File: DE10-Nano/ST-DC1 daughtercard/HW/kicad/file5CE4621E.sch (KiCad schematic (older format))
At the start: 18 parts, among them J10 ENC1_IN, J27 ENC2_IN, J3 ENC0_IN, J30 ENC3_IN, J33 ENC4_IN, J36 ENC5_IN, U1 AM26LS32, U10 AM26LS32, U11 AM26LS32, U12 AM26LS32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

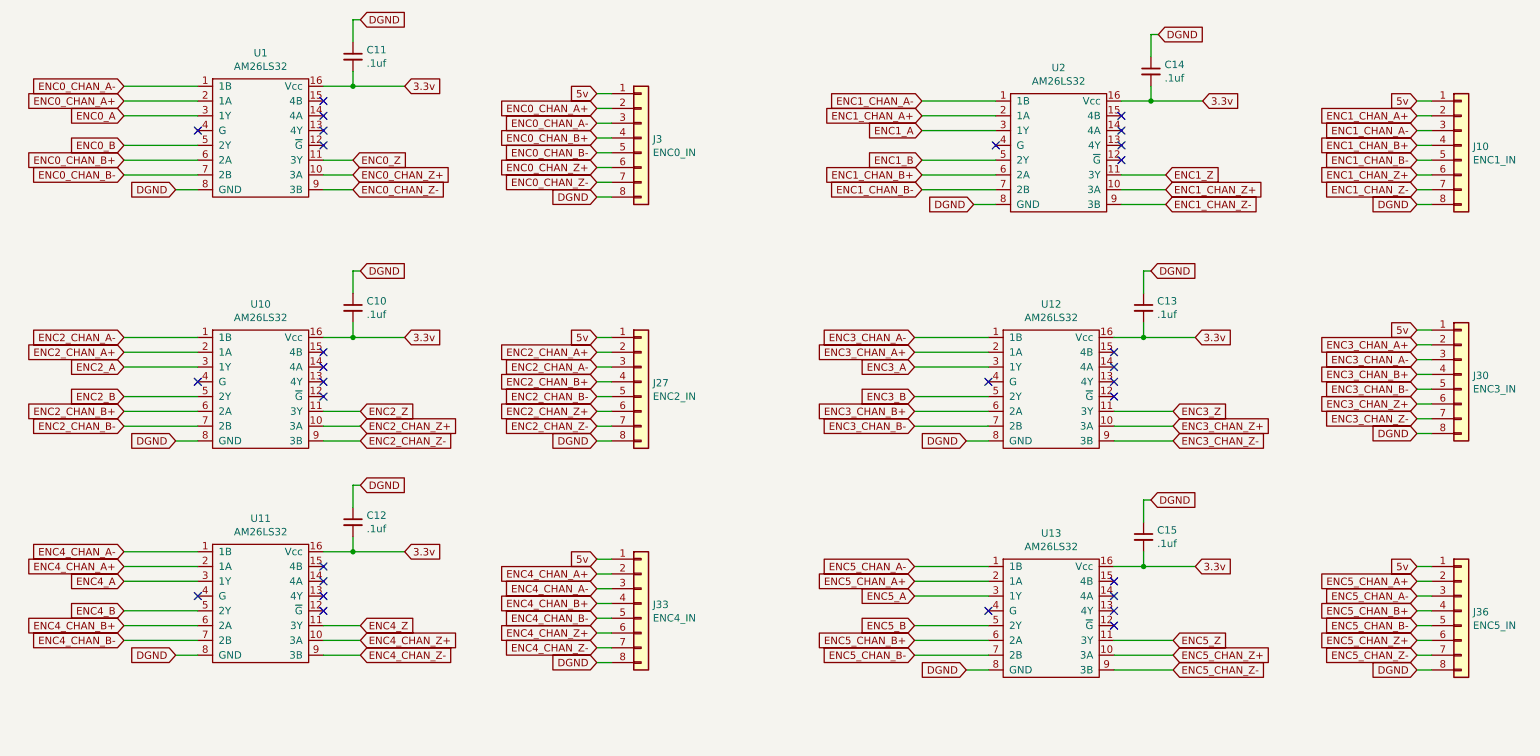
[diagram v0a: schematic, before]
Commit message: Add Artwork to PCB:   DE10-Nano/ST-DC1 daughtercard/HW/kicad/DE10nano interface-cache.lib 	Add Artwork to PCB:    DE10-Nano/ST-DC1 daughtercard/HW/kicad/DE10nano interface.jpg 	Add termination Resistors to diff inputs:   DE10-Nano/ST-DC1 daughtercard/HW/kicad/DE10nano interface.kicad_pcb 	Add termination Resistors to diff inputs:   DE10-Nano/ST-DC1 daughtercard/HW/kicad/DE10nano interface.kicad_pcb-bak 	Add termination Resistors to diff inputs:   DE10-Nano/ST-DC1 daughtercard/HW/kicad/DE10nano interface.net 	Add termination Resistors to diff inputs:   DE10-Nano/ST-DC1 daughtercard/HW/kicad/DE10nano interface.pro 	Add termination Resistors to diff inputs:   DE10-Nano/ST-DC1 daughtercard/HW/kicad/Images/DE10nano interface back.jpg 	Add Artwork to PCB:   DE10-Nano/ST-DC1 daughtercard/HW/kicad/Images/DE10nano interface.jpg 	Reflect incomplete BOM:    DE10-Nano/ST-DC1 daughtercard/HW/kicad/bom/BOM.ods -> DE10-Nano/ST-DC1 daughtercard/HW/kicad/bom/BOM-incomplete-use-ibom.ods 	Add termination Resistors to diff inputs:   DE10-Nano/ST-DC1 daughtercard/HW/kicad/bom/ibom.html 	Add termination Resistors to diff inputs:   DE10-Nano/ST-DC1 daughtercard/HW/kicad/file5CE4621E.sch 	Add termination Resistors to diff inputs:   DE10-Nano/ST-DC1 daughtercard/HW/kicad/file5CE4621E.sch-bak 	Add termination Resistors to diff inputs:   DE10-Nano/ST-DC1 daughtercard/HW/kicad/file5D10B445.sch-bak 	Add termination Resistors to diff inputs:   DE10-Nano/ST-DC1 daughtercard/HW/kicad/file5D22A4F0.sch 	modified:   DE10-Nano/ST-DC1 daughtercard/HW/kicad/file5D22A4F0.sch-bak 	modified:   DE10-Nano/ST-DC1 daughtercard/HW/kicad/gerbers rev_G.zip 	modified:   DE10-Nano/ST-DC1 daughtercard/HW/kicad/gerbers rev_G/DE10nano interface-B_Cu.gbr 	modified:   DE10-Nano/ST-DC1 daughtercard/HW/kicad/gerbers rev_G/DE10nano interface-B_Mask.gbr 	modified:   DE10-Nano/ST-DC1 daughtercard/HW/kicad/gerbers rev_G/DE10nano interface-B_Paste.gbr 	modified:   DE10-Nano/ST-DC1 daughtercard/HW/kicad/gerbers rev_G/DE10nano i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
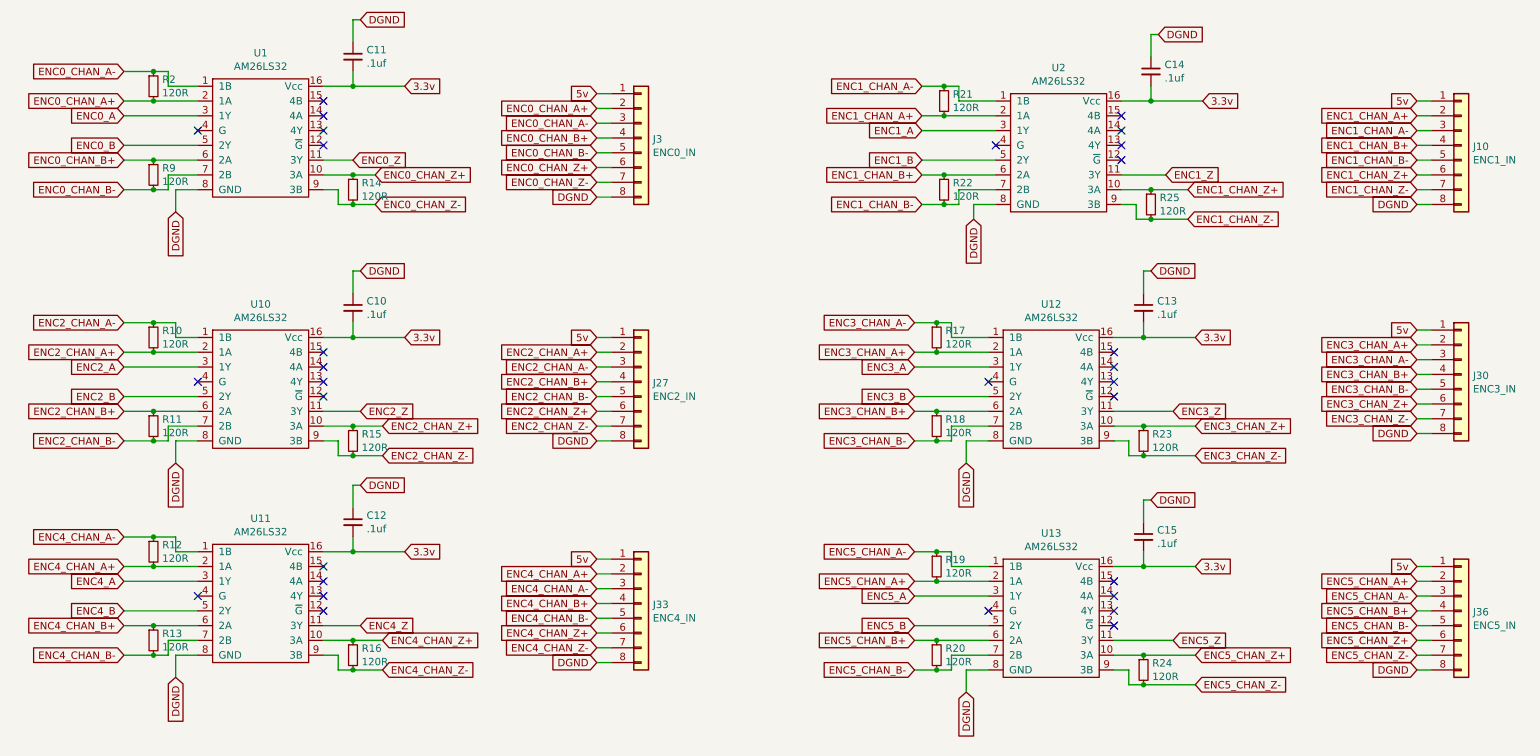
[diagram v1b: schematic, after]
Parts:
- added R10, R11, R12, R13, R14, R15, R16, R17, R18, R19, R2, R20, R21, R22, R23, R24, R25, R9: 120R, Resistor_SMD:R_0805_2012Metric, symbol Device:R_Small
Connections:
- net ENC0_CHAN_A+: now also R2.2
- net ENC0_CHAN_A-: now also R2.1
- net ENC0_CHAN_B+: now also R9.1
- net ENC0_CHAN_B-: now also R9.2
- net ENC0_CHAN_Z+: now also R14.1
- net ENC0_CHAN_Z-: now also R14.2
- net ENC1_CHAN_A+: now also R21.2
- net ENC1_CHAN_A-: now also R21.1
- net ENC1_CHAN_B+: now also R22.1
- net ENC1_CHAN_B-: now also R22.2
- net ENC1_CHAN_Z+: now also R25.1
- net ENC1_CHAN_Z-: now also R25.2
- net ENC2_CHAN_A+: now also R10.2
- net ENC2_CHAN_A-: now also R10.1
- net ENC2_CHAN_B+: now also R11.1
- net ENC2_CHAN_B-: now also R11.2
- net ENC2_CHAN_Z+: now also R15.1
- net ENC2_CHAN_Z-: now also R15.2
- net ENC3_CHAN_A+: now also R17.2
- net ENC3_CHAN_A-: now also R17.1
- net ENC3_CHAN_B+: now also R18.1
- net ENC3_CHAN_B-: now also R18.2
- net ENC3_CHAN_Z+: now also R23.1
- net ENC3_CHAN_Z-: now also R23.2
- net ENC4_CHAN_A+: now also R12.2
- net ENC4_CHAN_A-: now also R12.1
- net ENC4_CHAN_B+: now also R13.1
- net ENC4_CHAN_B-: now also R13.2
- net ENC4_CHAN_Z+: now also R16.1
- net ENC4_CHAN_Z-: now also R16.2
- net ENC5_CHAN_A+: now also R19.2
- net ENC5_CHAN_A-: now also R19.1
- net ENC5_CHAN_B+: now also R20.1
- net ENC5_CHAN_B-: now also R20.2
- net ENC5_CHAN_Z+: now also R24.1
- net ENC5_CHAN_Z-: now also R24.2
